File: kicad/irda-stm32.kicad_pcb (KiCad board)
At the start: 2 copper layers, 40 x 60 mm, 33 parts, among them J1 USB_C_Receptacle_USB2.0_16P, J2 UART, J3 SWD, SW1 BOOT0_BUT, SW2 NRST_BUT, U1 TLV1117LV33DCYR, U2 STM32F042K6Tx, U3 TFBS4711

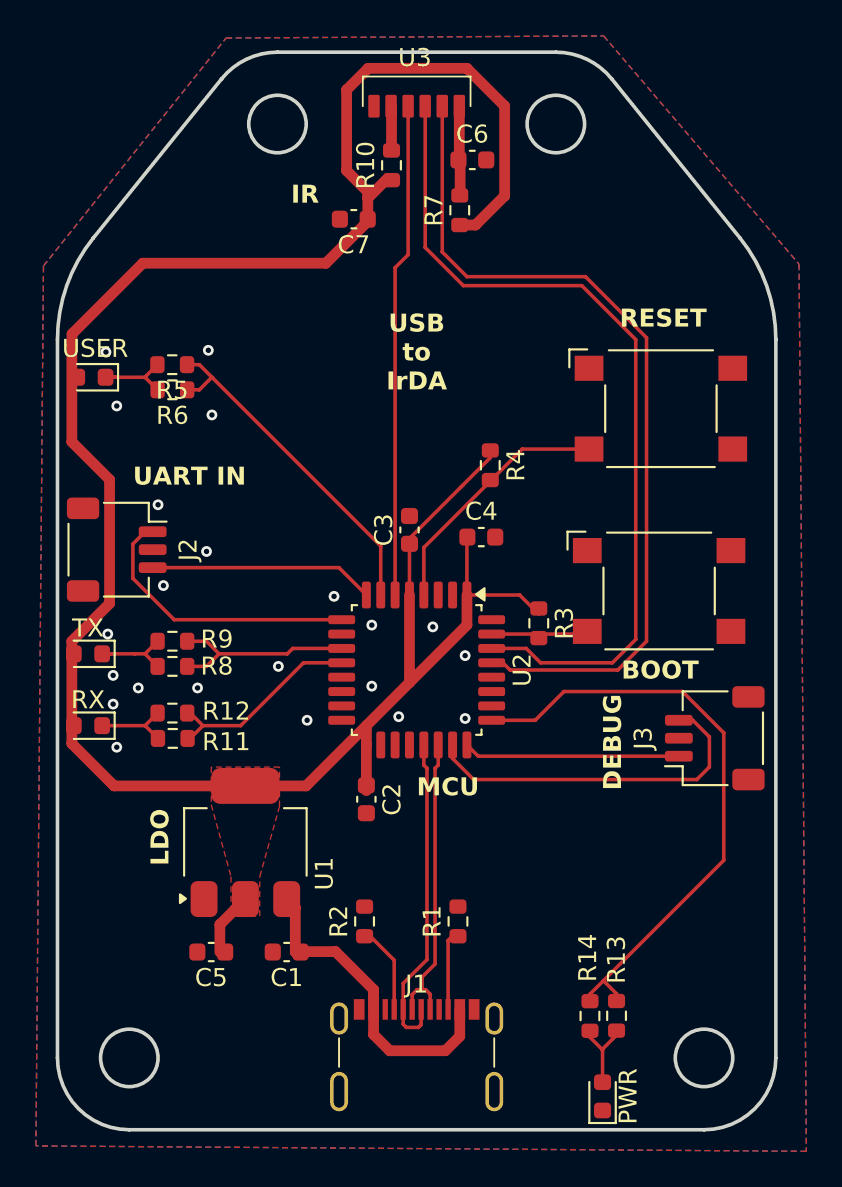
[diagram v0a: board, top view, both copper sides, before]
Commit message: add enclsoure
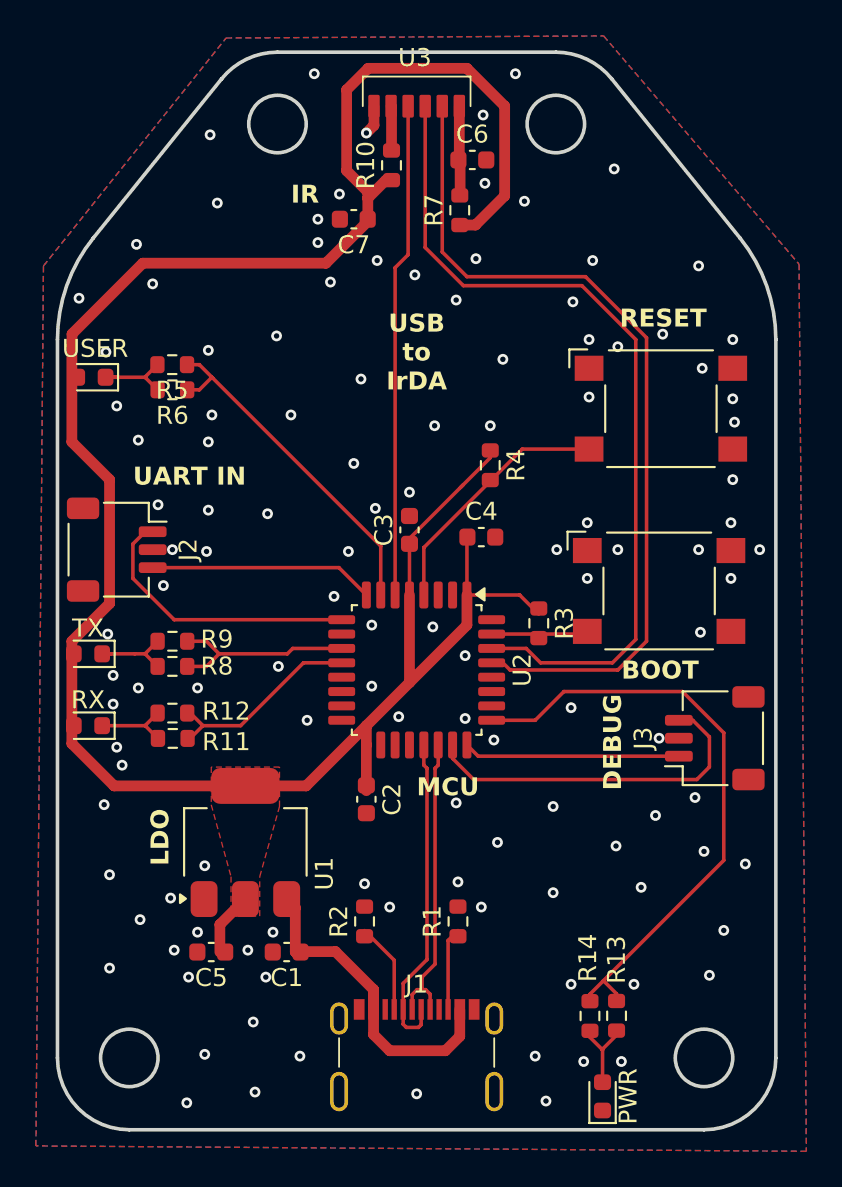
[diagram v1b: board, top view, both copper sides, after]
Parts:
- added REF**: Tab, PCM_kikit:Tab, F.Cu at (144.8, 77.0)
- added REF**: Tab, PCM_kikit:Tab, F.Cu at (184.8, 106.1)
- added REF**: Tab, PCM_kikit:Tab, F.Cu at (184.8, 77.0)
- added REF**: Tab, PCM_kikit:Tab, F.Cu at (144.8, 106.1)
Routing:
- net GND: track 0.00 -> 1.67 mm, vias 22 -> 122

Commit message: update kicad, idk
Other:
- board text added: "USB to IrDA v1"
- board text removed: "USB to IrDA"
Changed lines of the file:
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@@
 		)
 	)
-	(gr_text "USB\nto\nIrDA"
+	(gr_text "USB\nto\nIrDA\nv1"
 		(at 164.8 74.9 0)
 		(layer "F.SilkS")

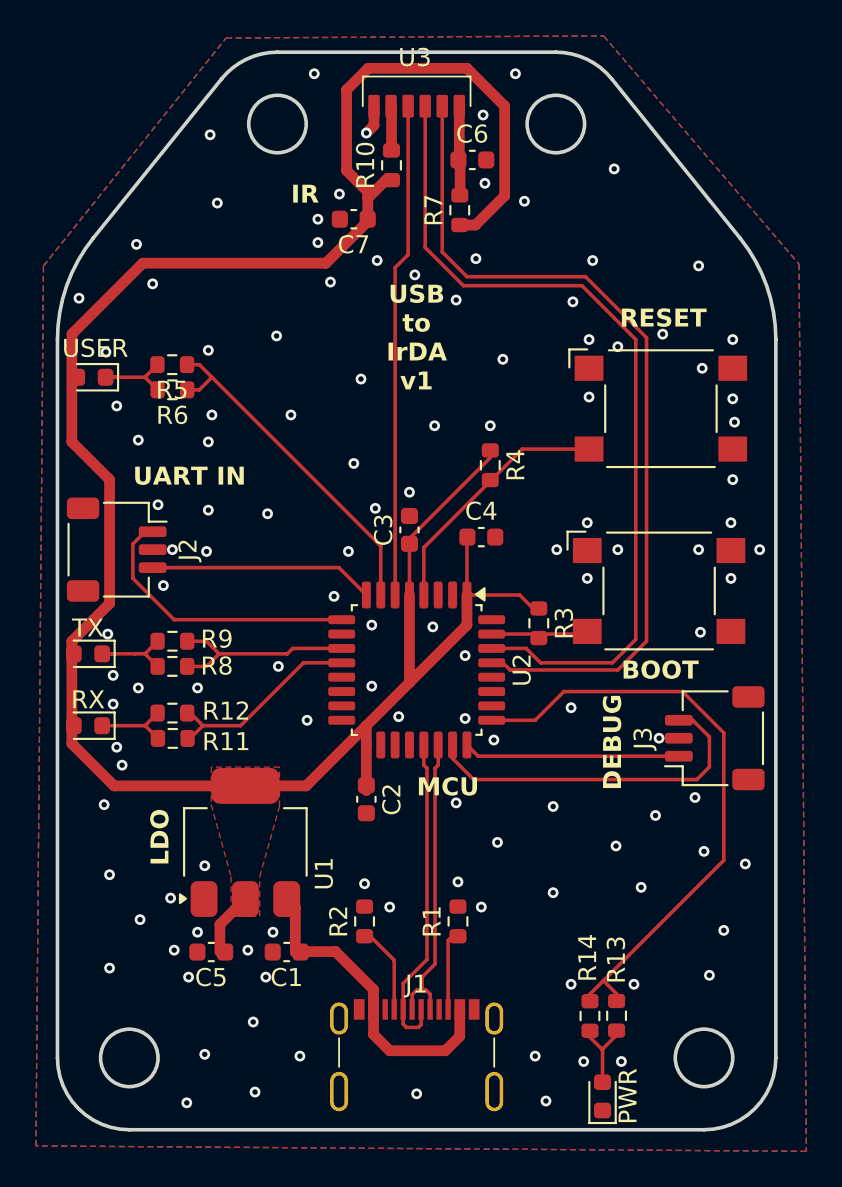
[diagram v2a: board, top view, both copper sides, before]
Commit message: update PCB for c071fbp6
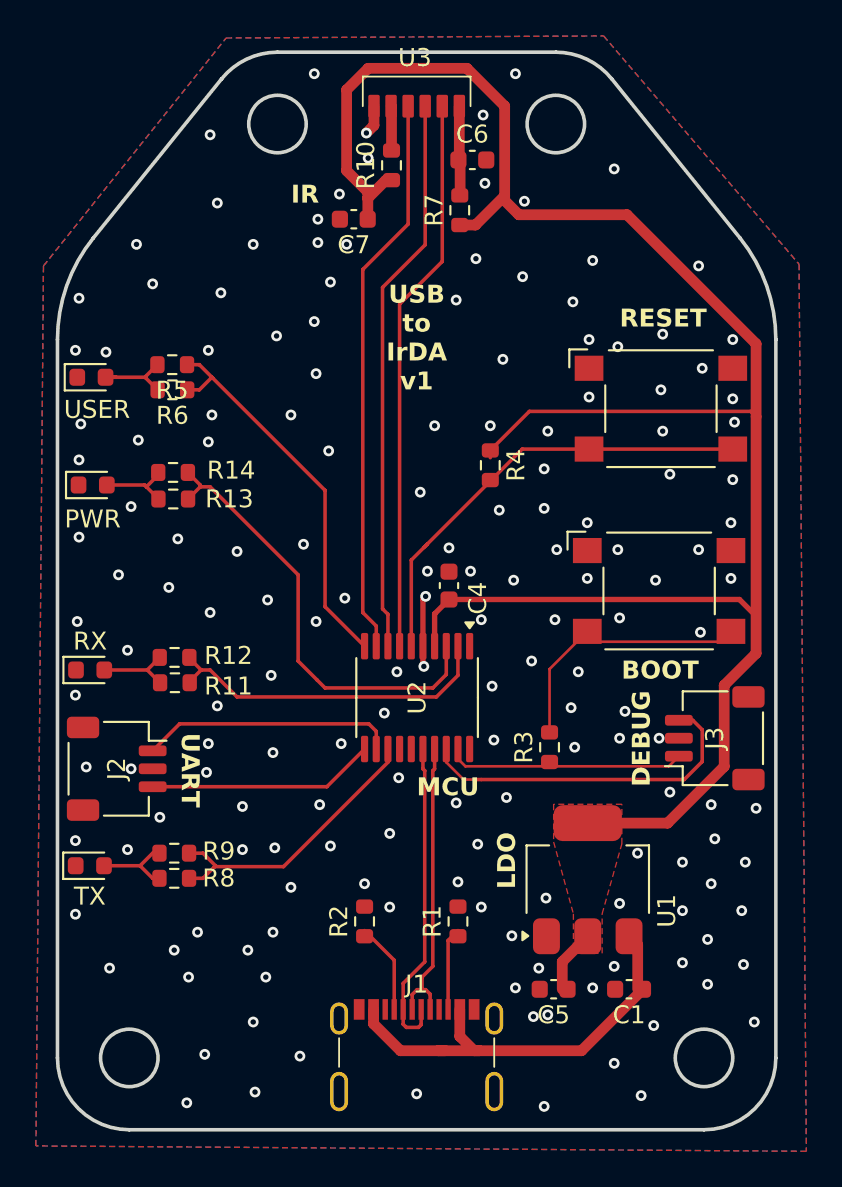
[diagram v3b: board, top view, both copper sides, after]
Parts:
- removed C2, C3: 4.7u, Capacitor_SMD:C_0603_1608Metric
- U2: value STM32F042K6Tx -> STM32C071FBPx; footprint Package_QFP:LQFP-32_7x7mm_P0.8mm -> Package_SO:TSSOP-20_4.4x6.5mm_P0.65mm
- moved D4 44.3 mm to (146.8, 80.1), turned to 0 degrees
- moved R14 38.1 mm to (151.2, 79.4), turned to 180 degrees
- moved R13 37.9 mm to (151.2, 80.9), turned to 180 degrees
- moved C1 19.2 mm to (176.6, 108.2)
- moved C5 19.2 mm to (172.4, 108.2)
- moved U1 19.2 mm to (174.3, 102.1)
- moved J2 12.2 mm to (148.1, 95.9)
- moved D2 11.8 mm to (146.6, 101.3), turned to 0 degrees
- moved R8 11.8 mm to (151.3, 102.0)
- moved R9 11.8 mm to (151.3, 100.6)
- moved R3 6.93 mm to (172.2, 94.7), turned to 90 degrees
- moved C4 3.24 mm to (166.6, 85.7), turned to 90 degrees
- moved D3 3.10 mm to (146.6, 90.4), turned to 0 degrees
- moved R11 3.10 mm to (151.3, 91.1)
- moved R12 3.10 mm to (151.3, 89.7)
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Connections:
- D1 pad 1: Net-(D1-K) -> GND
- D1 pad 2: +3.3V -> Net-(D1-A)
- D2 pad 1: Net-(D2-K) -> GND
- D2 pad 2: +3.3V -> Net-(D2-A)
- D3 pad 1: Net-(D3-K) -> GND
- D3 pad 2: +3.3V -> Net-(D3-A)
- R11 pad 1: /~{RX} -> /RX_LED
- R11 pad 2: Net-(D3-K) -> Net-(D3-A)
- R12 pad 1: /~{RX} -> /RX_LED
- R12 pad 2: Net-(D3-K) -> Net-(D3-A)
- R3 pad 1: +3.3V -> /SWCLK
- R3 pad 2: /BOOT0 -> Net-(R3-Pad2)
- R5 pad 1: /~{USER} -> /USER_LED
- R5 pad 2: Net-(D1-K) -> Net-(D1-A)
- R6 pad 1: /~{USER} -> /USER_LED
- R6 pad 2: Net-(D1-K) -> Net-(D1-A)
- R8 pad 1: /~{TX} -> /TX_LED
- R8 pad 2: Net-(D2-K) -> Net-(D2-A)
- R9 pad 1: /~{TX} -> /TX_LED
- R9 pad 2: Net-(D2-K) -> Net-(D2-A)
- SW1 pad 2: /BOOT0 -> Net-(R3-Pad2)
- U2 pad 1: +3.3V -> unconnected-(U2-PB7/PB8-Pad1)
- U2 pad 10: unconnected-(U2-PA4-Pad10) -> /USER_LED
- U2 pad 11: /~{TX} -> /EXT_TX
- U2 pad 12: /~{RX} -> /EXT_RX
- U2 pad 13: unconnected-(U2-PA7-Pad13) -> /TX_LED
- U2 pad 16: GND -> /USB_DN
- U2 pad 17: +3.3V -> /USB_DP
- U2 pad 18: unconnected-(U2-PA8-Pad18) -> /SWDIO
- U2 pad 19: unconnected-(U2-PA9-Pad19) -> /SWCLK
- U2 pad 2: unconnected-(U2-PF0-Pad2) -> /RX_LED
- U2 pad 3: unconnected-(U2-PF1-Pad3) -> /POWER_LED
- U2 pad 4: /NRST -> +3.3V
- U2 pad 5: +3.3V -> GND
- U2 pad 6: /IRDA_SD -> /NRST
- U2 pad 7: /~{USER} -> /IRDA_TX
- U2 pad 8: /EXT_TX -> /IRDA_RX
- U2 pad 9: /EXT_RX -> /IRDA_SD
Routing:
- net /USER_LED: track 0.00 -> 21.9 mm
- net /~{USER}: track 19.4 -> 0.00 mm
- net /RX_LED: track 0.00 -> 19.0 mm
- net /IRDA_TX: track 47.8 -> 31.1 mm
- net /TX_LED: track 0.00 -> 16.3 mm
- net /IRDA_RX: track 47.3 -> 31.2 mm
- net Net-(R3-Pad2): track 0.00 -> 15.2 mm
- net /~{RX}: track 11.5 -> 0.00 mm
- net /NRST: track 14.1 -> 25.5 mm
- net /~{TX}: track 11.1 -> 0.00 mm
- net +3.3V: track 129.3 -> 118.5 mm
- net /POWER_LED: track 34.0 -> 25.1 mm
- net /VUSB: track 18.9 -> 24.3 mm
- net /BOOT0: track 5.39 -> 0.00 mm
- net Net-(D2-K): track 5.36 -> 0.00 mm
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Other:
- board text added: "UART"
- board text removed: "UART IN"

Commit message: widen resistor spacing
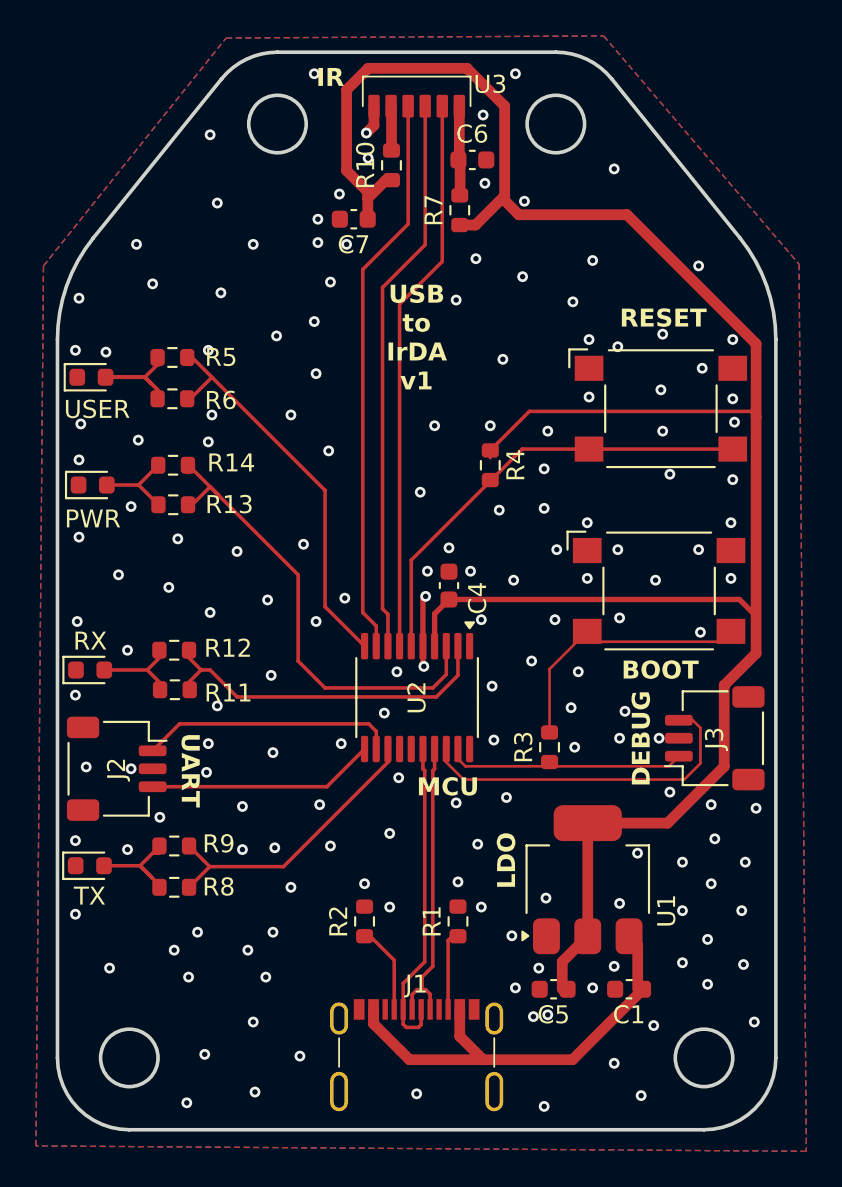
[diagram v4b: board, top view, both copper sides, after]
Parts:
- moved R6 0.50 mm to (151.2, 75.3)
- moved R8 0.50 mm to (151.3, 102.5)
- moved R12 0.40 mm to (151.3, 89.3)
- moved R5 0.40 mm to (151.2, 73.0)
- moved R14 0.40 mm to (151.2, 79.0)
- moved R9 0.40 mm to (151.3, 100.2)
- moved R11 0.39 mm to (151.3, 91.5)
- moved R13 0.32 mm to (151.2, 81.2)
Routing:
- net +3.3V: track 118.5 -> 124.8 mm
- net Net-(D1-A): track 5.12 -> 8.35 mm
- net /POWER_LED: track 25.1 -> 26.5 mm
- net Net-(D2-A): track 4.74 -> 5.94 mm
- net Net-(D4-A): track 4.52 -> 5.14 mm
- net /SWDIO: track 19.5 -> 19.0 mm
- removed copper zone on F.Cu, net +3.3V

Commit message: fix BOOT0 button and USB ground
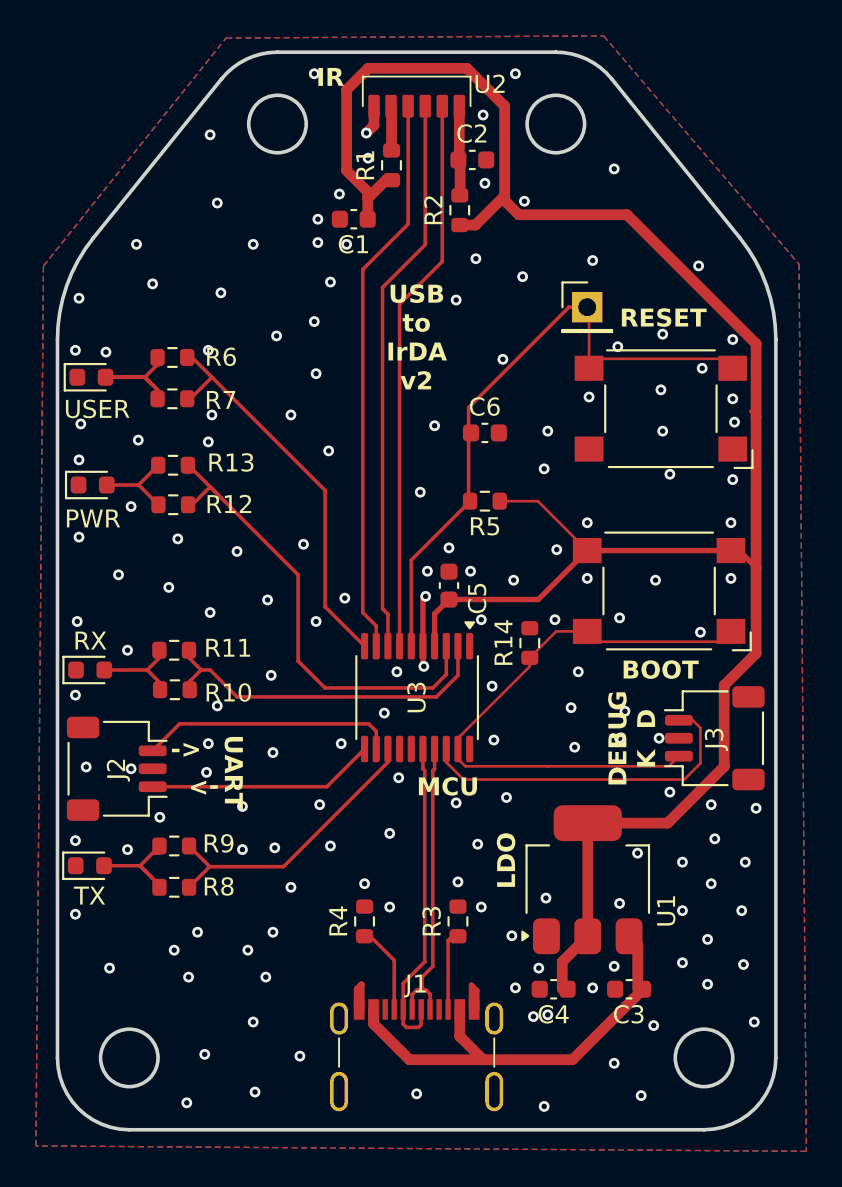
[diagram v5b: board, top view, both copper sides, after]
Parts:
- added C6: 0.1u, Capacitor_SMD:C_0603_1608Metric, F.Cu at (168.6, 77.2)
- added TP1: NRST, Connector_PinHeader_2.54mm:PinHeader_1x01_P2.54mm_Vertical, F.Cu at (174.3, 70.2)
- moved R14 5.90 mm to (171.1, 88.9)
- moved R5 2.02 mm to (168.6, 81.0), turned to 180 degrees
- turned SW1 to 180 degrees
- turned SW2 to 180 degrees
- renumbered C7 to C1, C6 to C2, C1 to C3, C5 to C4, C4 to C5, R10 to R1, R11 to R10, R12 to R11, R13 to R12, R14 to R13, R3 to R14, R7 to R2, R1 to R3, R2 to R4, R4 to R5, R5 to R6, R6 to R7, SW2 to SW1, SW1 to SW2, U3 to U2, U2 to U3
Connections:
- R14 pad 2: Net-(R3-Pad2) -> GND
- SW2 pad 1: GND -> /SWCLK
- SW2 pad 2: Net-(R3-Pad2) -> +3.3V
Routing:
- net /SWCLK: track 13.3 -> 32.5 mm
- net Net-(R3-Pad2): track 15.2 -> 0.00 mm
- net /NRST: track 25.3 -> 35.4 mm
- net +3.3V: track 124.8 -> 116.1 mm
- net GND: track 5.79 -> 11.6 mm, vias 170 -> 162
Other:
- board text added: "->"
- board text added: "D"
- board text added: "K"
- board text added: "USB to IrDA v2"
- board text removed: "USB to IrDA v1"

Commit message: add lcsc/jlc part numbers and fix ir filters
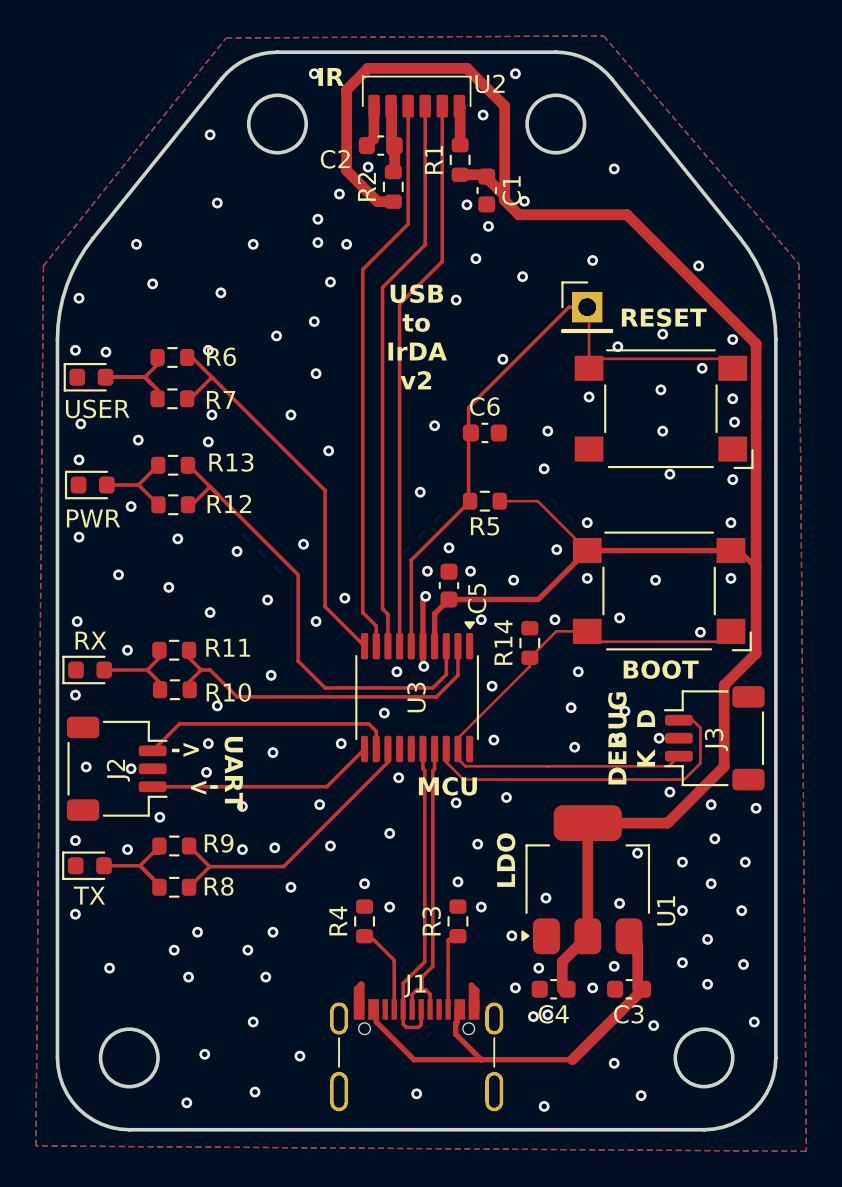
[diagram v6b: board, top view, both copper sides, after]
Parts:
- moved C2 4.37 mm to (162.8, 61.2)
- moved R1 2.80 mm to (167.2, 62.0)
- moved C1 1.88 mm to (168.7, 63.7), turned to -90 degrees
- moved R2 1.20 mm to (163.5, 63.5)
- renumbered C2 to C1, C1 to C2, R2 to R1, R1 to R2
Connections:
- C1 pad 1: Net-(U2-VCC2) -> +3.3V
- C2 pad 1: +3.3V -> Net-(U2-VCC1)
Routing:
- net Net-(U2-VCC2): track 4.99 -> 2.19 mm
- net +3.3V: track 116.1 -> 114.1 mm
- net Net-(U2-VCC1): track 2.48 -> 4.09 mm
- net GND: track 11.6 -> 12.3 mm
